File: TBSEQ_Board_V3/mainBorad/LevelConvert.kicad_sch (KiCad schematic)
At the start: 8 parts

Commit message: BoardV3
ERCチェック済
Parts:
- removed V05_IN_J, V05_OUT_J: Conn_01x03, Connector_PinSocket_1.27mm:PinSocket_1x03_P1.27mm_Vertical, symbol Connector_Generic:Conn_01x03
- removed V33_IN_J, V33_OUT_J1: Conn_01x05, Connector_PinHeader_1.27mm:PinHeader_1x05_P1.27mm_Vertical, symbol Connector_Generic:Conn_01x05
- added J10, J11: Conn_01x05, Connector_PinHeader_2.54mm:PinHeader_1x05_P2.54mm_Vertical, symbol Connector_Generic:Conn_01x05
- added J4, J5: Conn_01x03, Connector_PinHeader_2.54mm:PinHeader_1x03_P2.54mm_Vertical, symbol Connector_Generic:Conn_01x03
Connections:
- net at DgIC3.11 (Y7): now also J11.5 (Pin_5)
- net at DgIC3.12 (Y6): now also J11.4 (Pin_4)
- net at DgIC3.13 (Y5): now also J11.3 (Pin_3)
- net at DgIC3.14 (Y4): now also J11.2 (Pin_2)
- net at DgIC3.15 (Y3): now also J11.1 (Pin_1)
- net at DgIC3.5 (A3): now also J10.1 (Pin_1)
- net at DgIC3.6 (A4): now also J10.2 (Pin_2)
- net at DgIC3.7 (A5): now also J10.3 (Pin_3)
- net at DgIC3.8 (A6): now also J10.4 (Pin_4)
- net at DgIC3.9 (A7): now also J10.5 (Pin_5)
- net at DgIC2.13 (Y6): now also J5.1 (Pin_1)
- net at DgIC2.12 (Y7): now also J5.2 (Pin_2)
- net at DgIC2.11 (Y8): now also J5.3 (Pin_3)
- net at DgIC2.7 (A6): now also J4.1 (Pin_1)
- net at DgIC2.8 (A7): now also J4.2 (Pin_2)
- net at DgIC2.9 (A8): now also J4.3 (Pin_3)

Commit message: V3Board
アートワーク中
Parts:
- removed DgIC2: TC74VHC541FK, SamacSys_Parts:SOP50P400X100-20N, symbol SamacSys_Parts:TC74VHC541FK
- removed DgIC3: 74LVC541APW, SOP65P640X110-20N, symbol SamacSys_Parts:74LVC541APW
- removed J4, J5: Conn_01x03, Connector_PinHeader_2.54mm:PinHeader_1x03_P2.54mm_Vertical, symbol Connector_Generic:Conn_01x03
- added DgIC2, DgIC3: 74VHC541FT, SamacSys_Parts:SOP65P640X120-20N, symbol SamacSys_Parts:74VHC541FT
- added J4, J5: Conn_01x02, Connector_PinHeader_2.54mm:PinHeader_1x02_P2.54mm_Vertical, symbol Connector_Generic:Conn_01x02
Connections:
- net A+GATE: now also DgIC2.18 (Y1)
- net A+SLIDE: now also DgIC2.17 (Y2)
- net A+SyncOut: now also DgIC2.15 (Y4)
- net A+SyncOut_Run/Stop: now also DgIC2.14 (Y5)
- net A-ACC: now also DgIC2.16 (Y3)
- net D+3.3V: now also DgIC3.20 (VCC)
- net D+3.3V_MIDIRX: now also DgIC3.18 (Y1)
- net D+5V: now also DgIC2.20 (VCC)
- net D+5V_MIDIRx: now also DgIC3.2 (A1)
- net D+5V_SyncIn: now also DgIC3.3 (A2)
- net D+5V_SyncIn_Run/Stop: now also DgIC3.4 (A3)
- net D+GATE: now also DgIC2.2 (A1)
- net D+SLIDE: now also DgIC2.3 (A2)
- net D+SyncIn: now also DgIC3.17 (Y2)
- net D+SyncIn_Run/Stop: now also DgIC3.16 (Y3)
- net D+SyncOut: now also DgIC2.5 (A4)
- net D+SyncOut_Run/Stop: now also DgIC2.6 (A5)
- net D-ACC: now also DgIC2.4 (A3)
- net GNDD: now also DgIC2.1 (~{G1}), DgIC2.10 (GND), DgIC2.19 (~{G2}), DgIC3.1 (~{G1}), DgIC3.10 (GND), DgIC3.19 (~{G2})
- net at J11.5 (Pin_5): now also DgIC3.11 (Y8)
- net at J11.4 (Pin_4): now also DgIC3.12 (Y7)
- net at J11.3 (Pin_3): now also DgIC3.13 (Y6)
- net at J11.2 (Pin_2): now also DgIC3.14 (Y5)
- net at J11.1 (Pin_1): now also DgIC3.15 (Y4)
- net at J10.1 (Pin_1): now also DgIC3.5 (A4)
- net at J10.2 (Pin_2): now also DgIC3.6 (A5)
- net at J10.3 (Pin_3): now also DgIC3.7 (A6)
- net at J10.4 (Pin_4): now also DgIC3.8 (A7)
- net at J10.5 (Pin_5): now also DgIC3.9 (A8)
- new net: DgIC2.12 (Y7), J5.1 (Pin_1)
- new net: DgIC2.11 (Y8), J5.2 (Pin_2)
- new net: DgIC2.8 (A7), J4.1 (Pin_1)
- new net: DgIC2.9 (A8), J4.2 (Pin_2)
- new net D+3.3V_MIDITX: DgIC2.7 (A6)
- new net D+5V_MIDITX: DgIC2.13 (Y6)
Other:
- moved on the sheet: J10

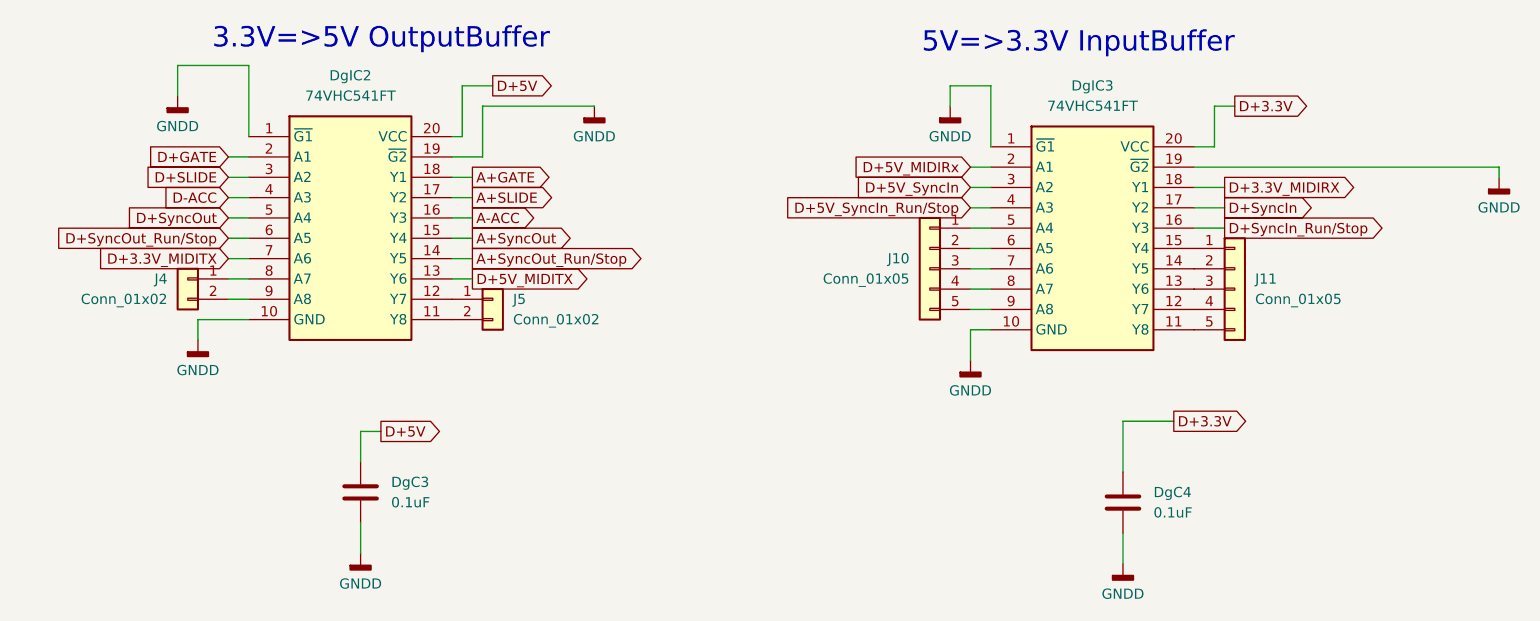
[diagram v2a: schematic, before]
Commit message: V3Board
ERCチェック修正中
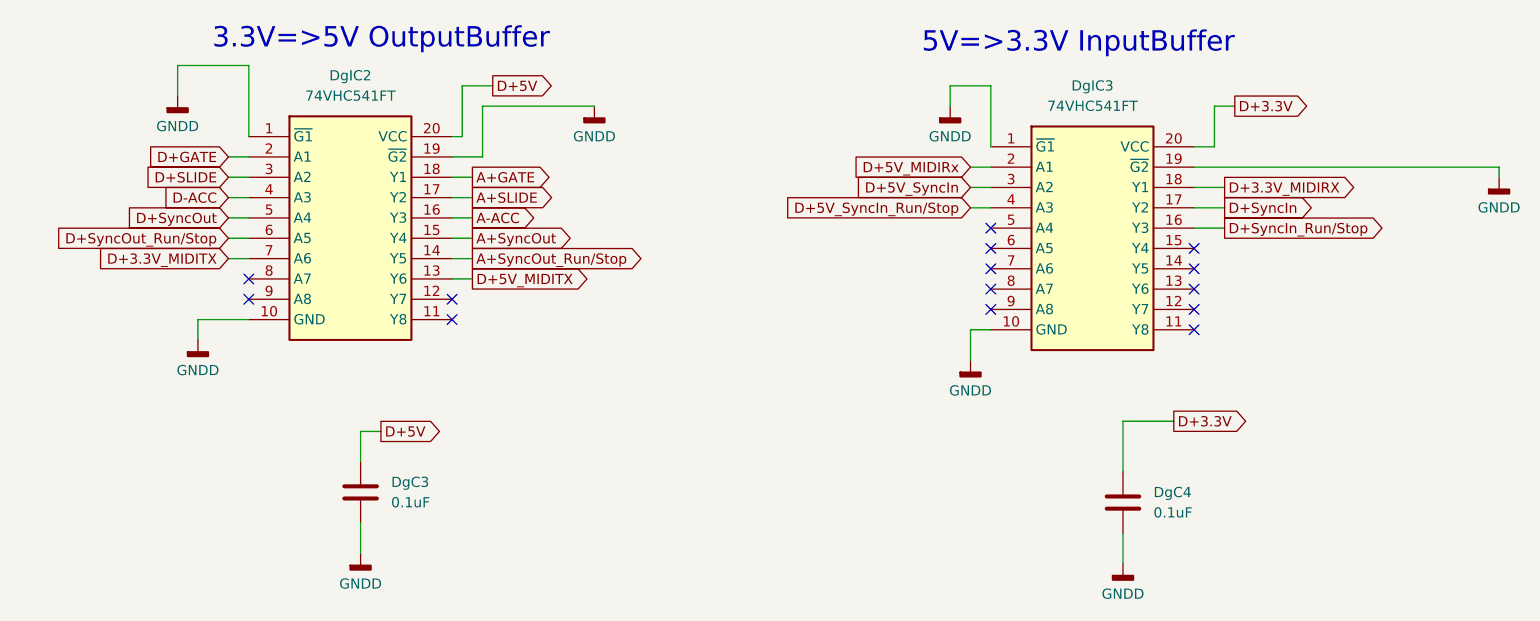
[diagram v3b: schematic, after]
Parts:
- removed J10, J11: Conn_01x05, Connector_PinHeader_2.54mm:PinHeader_1x05_P2.54mm_Vertical, symbol Connector_Generic:Conn_01x05
- removed J4, J5: Conn_01x02, Connector_PinHeader_2.54mm:PinHeader_1x02_P2.54mm_Vertical, symbol Connector_Generic:Conn_01x02
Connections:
- no-connect marks 0 -> 14
